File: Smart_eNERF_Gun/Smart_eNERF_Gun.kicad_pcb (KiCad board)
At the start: 2 copper layers, 55 x 62 mm, 25 parts, among them T32 Teensy32

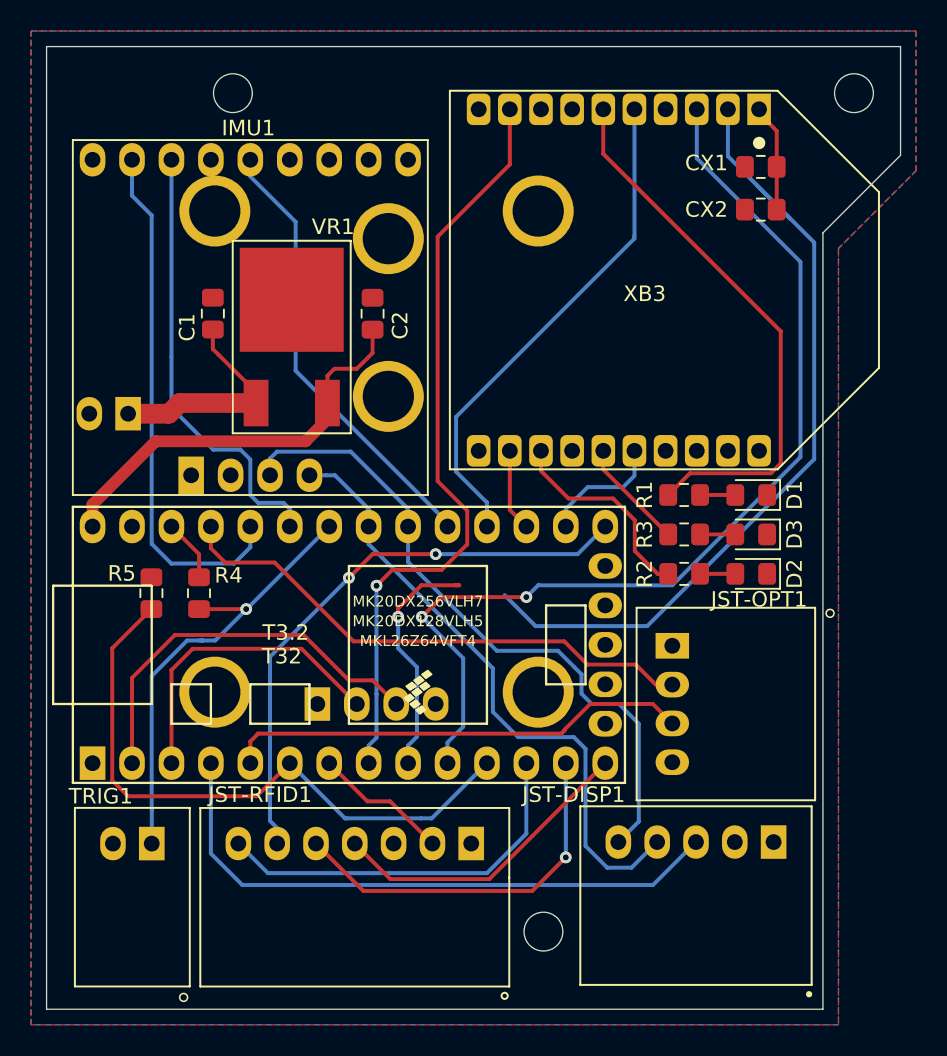
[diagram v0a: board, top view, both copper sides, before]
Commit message: Update routes and silk screen
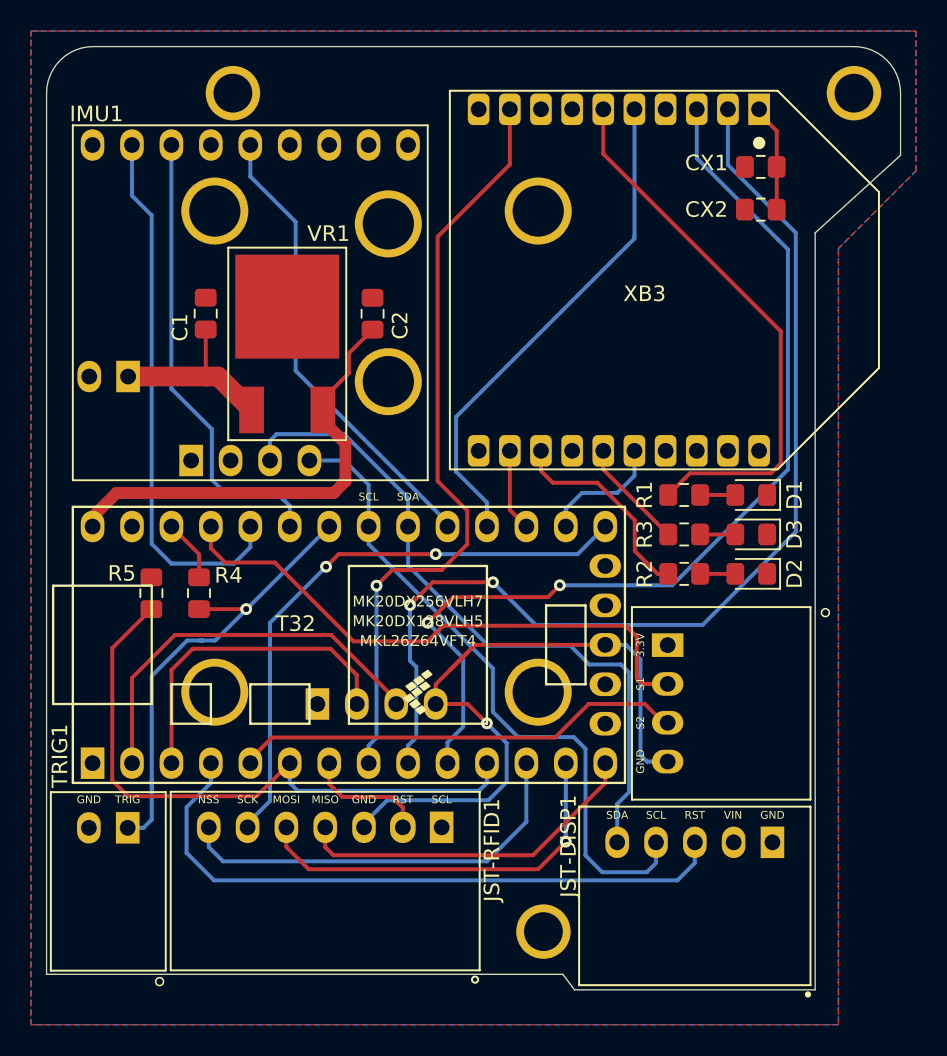
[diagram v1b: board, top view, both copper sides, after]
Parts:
- H1, H2, H3: footprint MountingHole:MountingHole_2.5mm -> Smart_eNERF_Gun:Mount_2.5mm
- moved SUP1 2.40 mm to (54.0, 86.2)
- moved JST-RFID1 2.17 mm to (67.9, 118.7)
- moved TRIG1 1.85 mm to (54.0, 115.3)
- moved IMU1 0.95 mm to (63.1, 81.5)
- moved VR1 0.53 mm to (65.5, 81.8)
- moved C1 0.46 mm to (60.2, 82.2)
- moved JST-OPT1 0.30 mm to (90.0, 107.3)
- moved JST-DISP1 0.08 mm to (91.8, 116.2)
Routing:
- net GND: track 0.00 -> 44.3 mm, vias 0 -> 1
- net /OPT-S1: track 34.8 -> 38.1 mm
- net +5V: track 26.9 -> 29.8 mm
- net /DISP-RST: track 39.0 -> 41.9 mm
- net /I2C-SCL: track 40.4 -> 43.3 mm
- net /RFID-MISO: track 20.2 -> 22.7 mm
- net /RFID-NSS: track 24.9 -> 26.9 mm
- net /I2C-SDA: track 43.2 -> 45.1 mm
- net +BATT: track 14.5 -> 12.6 mm
- net /T32-2-XB: track 64.8 -> 63.3 mm
- net /RFID-MOSI: track 24.3 -> 25.6 mm
- net /IMU-INT1: track 28.8 -> 30.0 mm
- net /T32-2-GPS: track 20.0 -> 21.1 mm
- net /OPT-S2: track 30.1 -> 29.1 mm
- net /GPS-2-T32: track 25.5 -> 26.3 mm
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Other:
- board size 55 x 62 mm -> 55 x 60.8 mm
- board text added: "3.3V"
- board text added: "GND"
- board text added: "MISO"
- board text added: "MOSI"
- board text added: "NSS"
- board text added: "RST"
- board text added: "S1"
- board text added: "S2"
- board text added: "SCK"
- board text added: "SCL"
- board text added: "SDA"
- board text added: "TRIG"
- board text added: "VIN"
- board text removed: "Are you Smart eNERF?"

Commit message: Production 6.2 commit for sensor stick
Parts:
- removed IMU1: LSM9D61, Smart_eNERF_Gun:LSM9D61_Breakout
- added 9DOF Sensor: LSM9DS1_Sensor_Stick, Smart_eNERF_Gun:LSM9DOF_Sensor_Stick, F.Cu at (63.1, 88.0)
- added I2C-Header1: 4-pin-header-i2c, Smart_eNERF_Gun:4-pin-i2c-header, F.Cu at (71.5, 73.0)
- added Pin1: 2-pin-power, Smart_eNERF_Gun:2-pin-power, F.Cu at (66.5, 72.7)
- Teensy 3.2 µC: renamed from T32
- XBee 3.0 RF Module: renamed from XB3
- moved SUP1 5.75 mm to (54.0, 80.5)
- moved CX1 4.40 mm to (91.6, 72.5)
- moved CX2 4.40 mm to (91.6, 75.3)
- moved C1 1.86 mm to (58.4, 82.5)
- moved VR1 1.72 mm to (64.4, 83.1)
- moved D2 1.08 mm to (94.5, 99.6)
- moved R2 1.08 mm to (90.2, 99.6)
- moved C2 0.96 mm to (70.1, 82.5)
- moved D3 0.95 mm to (94.5, 96.7)
- moved R3 0.95 mm to (90.2, 96.7)
- moved D1 0.90 mm to (94.5, 93.9)
- moved R1 0.90 mm to (90.2, 93.9)
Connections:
- Teensy 3.2 µC pad 24: /IMU-M-RDY -> Net-(T32-Pad24)
- Teensy 3.2 µC pad 28: /IMU-INT1 -> Net-(T32-Pad28)
- Teensy 3.2 µC pad 29: /IMU-INT2 -> Net-(T32-Pad29)
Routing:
- net /IMU-INT2: track 33.9 -> 0.00 mm
- net /IMU-INT1: track 30.0 -> 0.00 mm
- net /IMU-M-RDY: track 28.9 -> 0.00 mm
- net +5V: track 29.8 -> 51.2 mm, vias 0 -> 1
- net /I2C-SCL: track 43.3 -> 63.0 mm
- net /I2C-SDA: track 45.1 -> 58.8 mm
- net +BATT: track 12.6 -> 16.2 mm
- net /XB-RSSI: track 35.6 -> 38.8 mm
- net +3V3: track 10.9 -> 14.1 mm
- net /T32-2-XB: track 63.3 -> 64.9 mm
- net /XB-ASOC: track 7.12 -> 7.90 mm
- net /XB-WAKE: track 49.3 -> 48.6 mm
- net /XB-2-T32: track 68.7 -> 69.4 mm
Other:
- outline, holes or cut-outs redrawn
- board text added: "ASOC"
- board text added: "BAT+"
- board text added: "I2C"
- board text added: "ON"
- board text added: "RSSI"
- board text added: "Smart eNERF Gun"
- board text added: "T32-PWR"
- board text added: "µVIN"

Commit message: Production
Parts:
- removed 9DOF Sensor: LSM9DS1_Sensor_Stick, Smart_eNERF_Gun:LSM9DOF_Sensor_Stick
- removed I2C-Header1: 4-pin-header-i2c, Smart_eNERF_Gun:4-pin-i2c-header
- removed Pin1: 2-pin-power, Smart_eNERF_Gun:2-pin-power
- added IMU1: LSM9D61, Smart_eNERF_Gun:LSM9D61_Breakout, F.Cu at (62.7, 81.8)
- T32: renamed from Teensy 3.2 µC
- XBee 3 RF Module: renamed from XBee 3.0 RF Module
- moved C2 9.52 mm to (72.1, 91.8), turned to 0 degrees
- moved SUP1 7.20 mm to (54.0, 87.7)
- moved C1 2.50 mm to (59.5, 84.8)
- moved VR1 1.27 mm to (65.1, 82.0)
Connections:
- T32 pad 24: Net-(T32-Pad24) -> /I2C-M-RDY
- T32 pad 28: Net-(T32-Pad28) -> /IMU-INT1
- T32 pad 29: Net-(T32-Pad29) -> /IMU-INT2
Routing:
- net /IMU-INT1: track 0.00 -> 32.6 mm
- net /IMU-INT2: track 0.00 -> 31.2 mm
- net /I2C-M-RDY: track 0.00 -> 29.6 mm
- net +5V: track 51.2 -> 26.3 mm, vias 1 -> 0
- net /I2C-SCL: track 63.0 -> 43.2 mm
- net /I2C-SDA: track 58.8 -> 44.8 mm
- net +BATT: track 16.2 -> 11.1 mm
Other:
- outline, holes or cut-outs redrawn
- board text removed: "I2C"
- board text removed: "T32-PWR"
- board text removed: "µVIN"
